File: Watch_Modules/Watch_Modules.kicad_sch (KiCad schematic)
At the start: 1 part, among them J1 Conn_01x06_Female

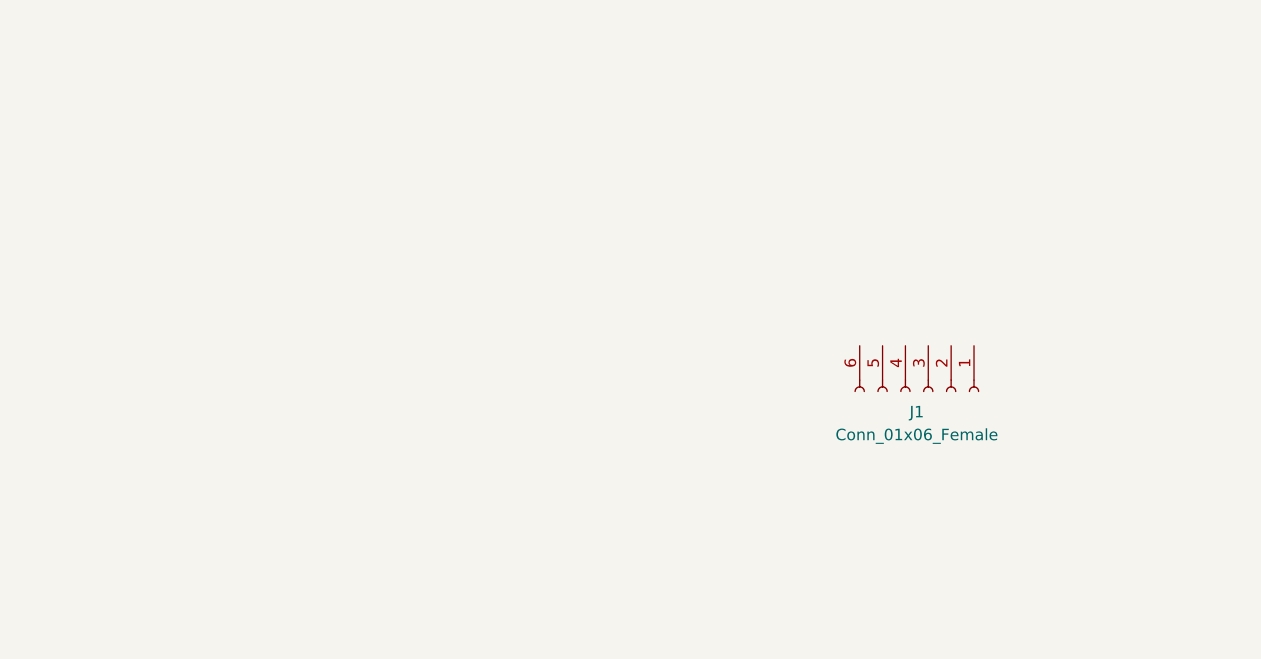
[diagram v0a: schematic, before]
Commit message: Graphical fixes, minor electrical fixes and enviro sensor module trial
Fixed some component values and added i2c pullups
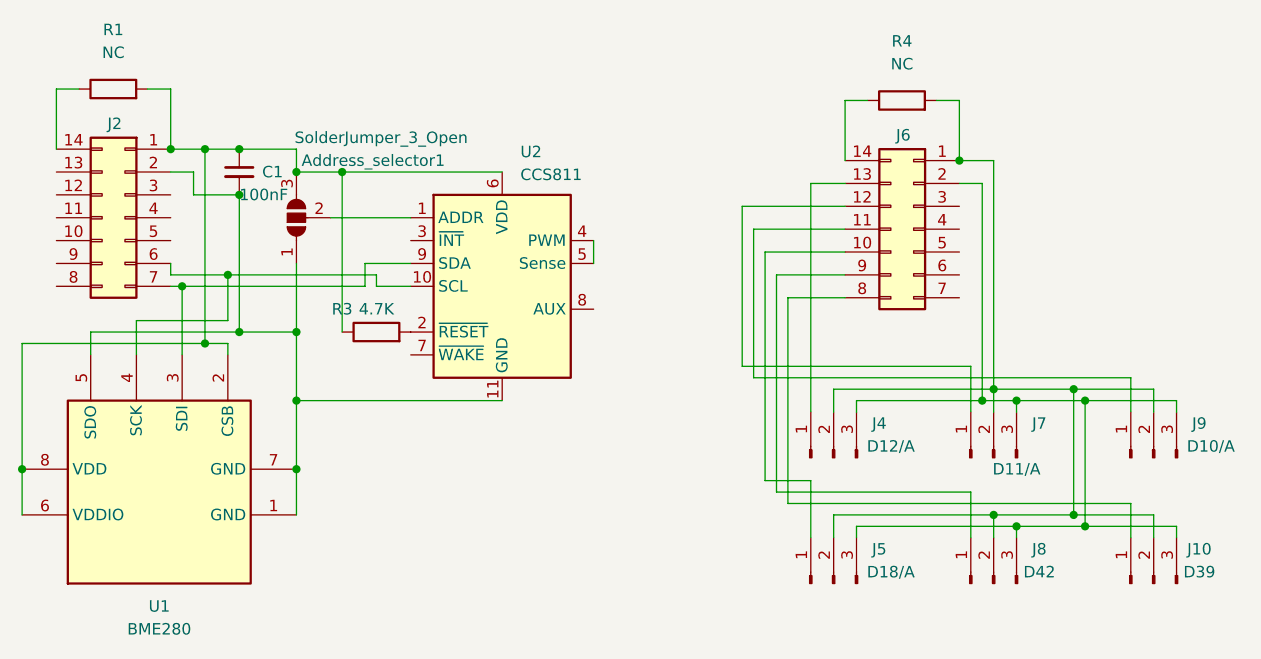
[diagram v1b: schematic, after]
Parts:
- removed J1: Conn_01x06_Female, 70AAJ-6-M0G:ModuleConnector, symbol Connector:Conn_01x06_Female
- added Address_selector1: SolderJumper_3_Open, Jumper:SolderJumper-3_P1.3mm_Open_RoundedPad1.0x1.5mm, symbol Jumper:SolderJumper_3_Open
- added C1: 100nF, Capacitor_SMD:C_0805_2012Metric, symbol Device:C_Small
- added J10: D39, Connector_PinHeader_2.54mm:PinHeader_1x03_P2.54mm_Vertical, symbol Connector:Conn_01x03_Male
- added J2, J6: Conn_02x07_Counter_Clockwise, Connector_PinHeader_1.27mm:PinHeader_2x07_P1.27mm_Horizontal, symbol Connector_Generic:Conn_02x07_Counter_Clockwise
- added J4: D12/A, Connector_PinHeader_2.54mm:PinHeader_1x03_P2.54mm_Vertical, symbol Connector:Conn_01x03_Male
- added J5: D18/A, Connector_PinHeader_2.54mm:PinHeader_1x03_P2.54mm_Vertical, symbol Connector:Conn_01x03_Male
- added J7: D11/A, Connector_PinHeader_2.54mm:PinHeader_1x03_P2.54mm_Vertical, symbol Connector:Conn_01x03_Male
- added J8: D42, Connector_PinHeader_2.54mm:PinHeader_1x03_P2.54mm_Vertical, symbol Connector:Conn_01x03_Male
- added J9: D10/A, Connector_PinHeader_2.54mm:PinHeader_1x03_P2.54mm_Vertical, symbol Connector:Conn_01x03_Male
- added R1, R4: NC, Resistor_SMD:R_0805_2012Metric, symbol Device:R
- added R3: 4.7K, Resistor_SMD:R_0805_2012Metric, symbol Device:R
- added U1: BME280, Package_LGA:Bosch_LGA-8_2.5x2.5mm_P0.65mm_ClockwisePinNumbering, symbol Sensor:BME280
- added U2: CCS811, Package_LGA:AMS_LGA-10-1EP_2.7x4mm_P0.6mm, symbol Sensor_Gas:CCS811
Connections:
- new net: J6.12 (Pin_12), J7.1 (Pin_1)
- new net: J10.2 (Pin_2), J4.2 (Pin_2), J5.2 (Pin_2), J6.1 (Pin_1), J7.2 (Pin_2), J8.2 (Pin_2), J9.2 (Pin_2), R4.2
- new net: J10.3 (Pin_3), J4.3 (Pin_3), J5.3 (Pin_3), J6.2 (Pin_2), J7.3 (Pin_3), J8.3 (Pin_3), J9.3 (Pin_3)
- new net: J6.11 (Pin_11), J9.1 (Pin_1)
- new net: J6.9 (Pin_9), J8.1 (Pin_1)
- new net: Address_selector1.1 (A), C1.2, J2.2 (Pin_2), U1.1 (GND), U1.5 (SDO), U1.7 (GND), U2.11 (GND)
- new net: Address_selector1.2 (C), U2.1 (ADDR)
- new net: Address_selector1.3 (B), C1.1, J2.1 (Pin_1), R1.2, R3.1, U1.2 (CSB), U1.6 (VDDIO), U1.8 (VDD), U2.6 (VDD)
- new net: J2.14 (Pin_14), R1.1
- new net: R3.2, U2.2 (~{RESET})
- new net: J5.1 (Pin_1), J6.10 (Pin_10)
- new net: J2.6 (Pin_6), U1.4 (SCK), U2.10 (SCL)
- new net: J2.7 (Pin_7), U1.3 (SDI), U2.9 (SDA)
- new net: J10.1 (Pin_1), J6.8 (Pin_8)
- new net: J4.1 (Pin_1), J6.13 (Pin_13)
- new net: U2.4 (PWM), U2.5 (Sense)
- new net: J6.14 (Pin_14), R4.1
